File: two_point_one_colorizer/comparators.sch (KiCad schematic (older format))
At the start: 13 parts, among them U7 LM393

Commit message: revised all boards
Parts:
- RV1, RV2: value 10k -> 10k_pot
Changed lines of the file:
@@
 P 3875 2675
 F 0 "RV1" H 3805 2721 50  0000 R CNN
-F 1 "10k" H 3805 2630 50  0000 R CNN
+F 1 "10k_pot" H 3805 2630 50  0000 R CNN
 F 2 "lib_fp:Potentiometer_Vertical_Large" H 3875 2675 50  0001 C CNN
 F 3 "~" H 3875 2675 50  0001 C CNN
@@
 P 3825 5175
 F 0 "RV2" H 3755 5221 50  0000 R CNN
-F 1 "10k" H 3755 5130 50  0000 R CNN
+F 1 "10k_pot" H 3755 5130 50  0000 R CNN
 F 2 "lib_fp:Potentiometer_Vertical_Large" H 3825 5175 50  0001 C CNN
 F 3 "~" H 3825 5175 50  0001 C CNN

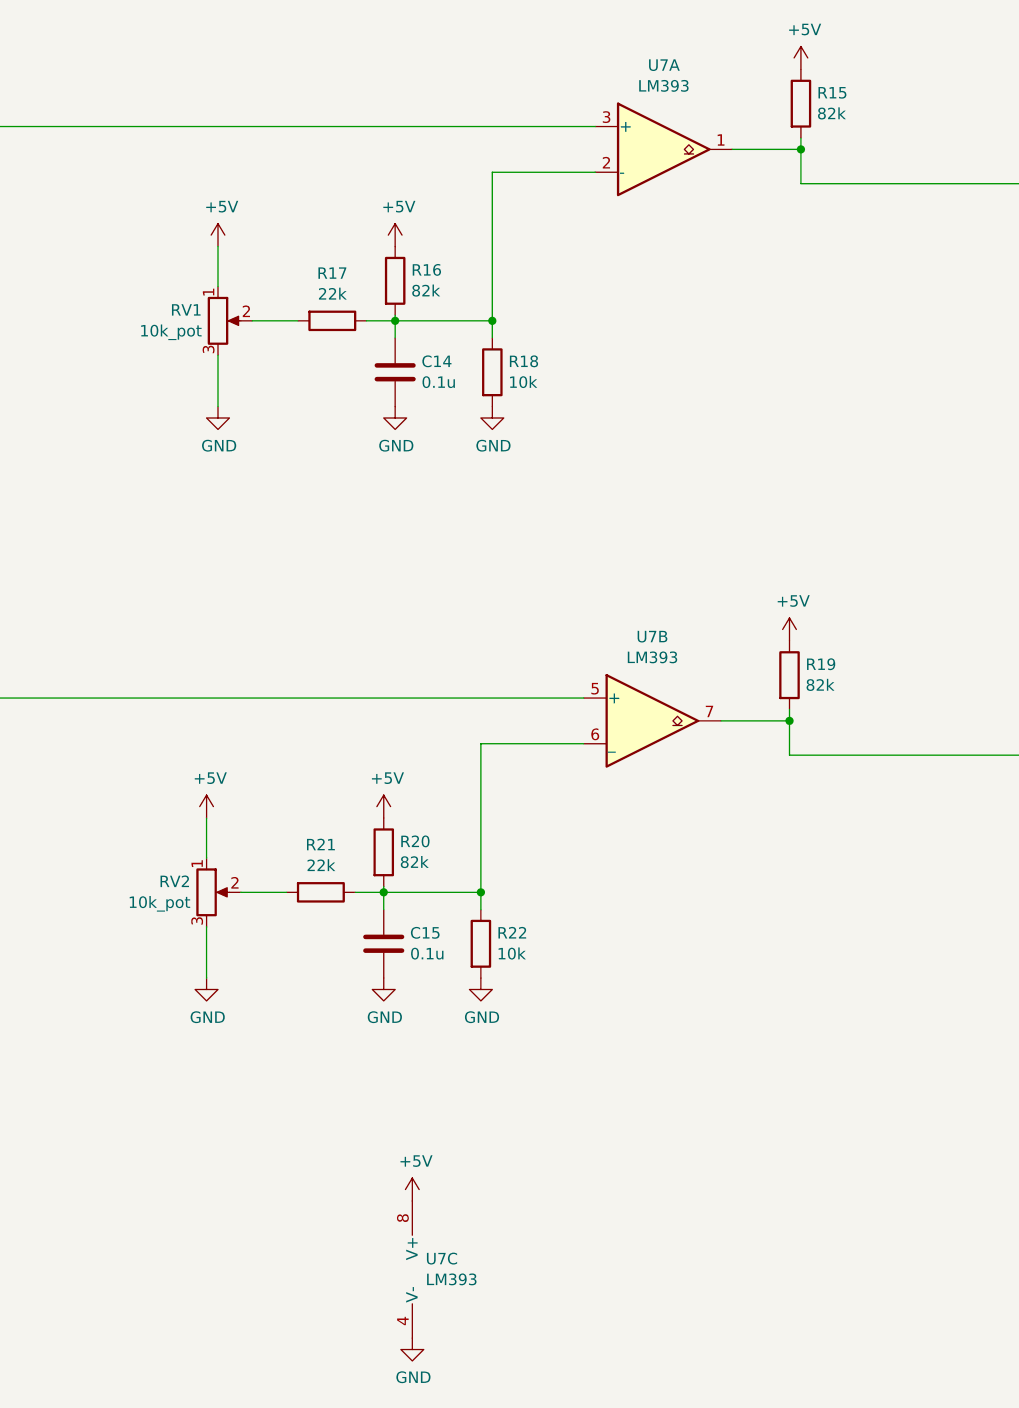
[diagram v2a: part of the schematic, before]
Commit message: lay out colorizer
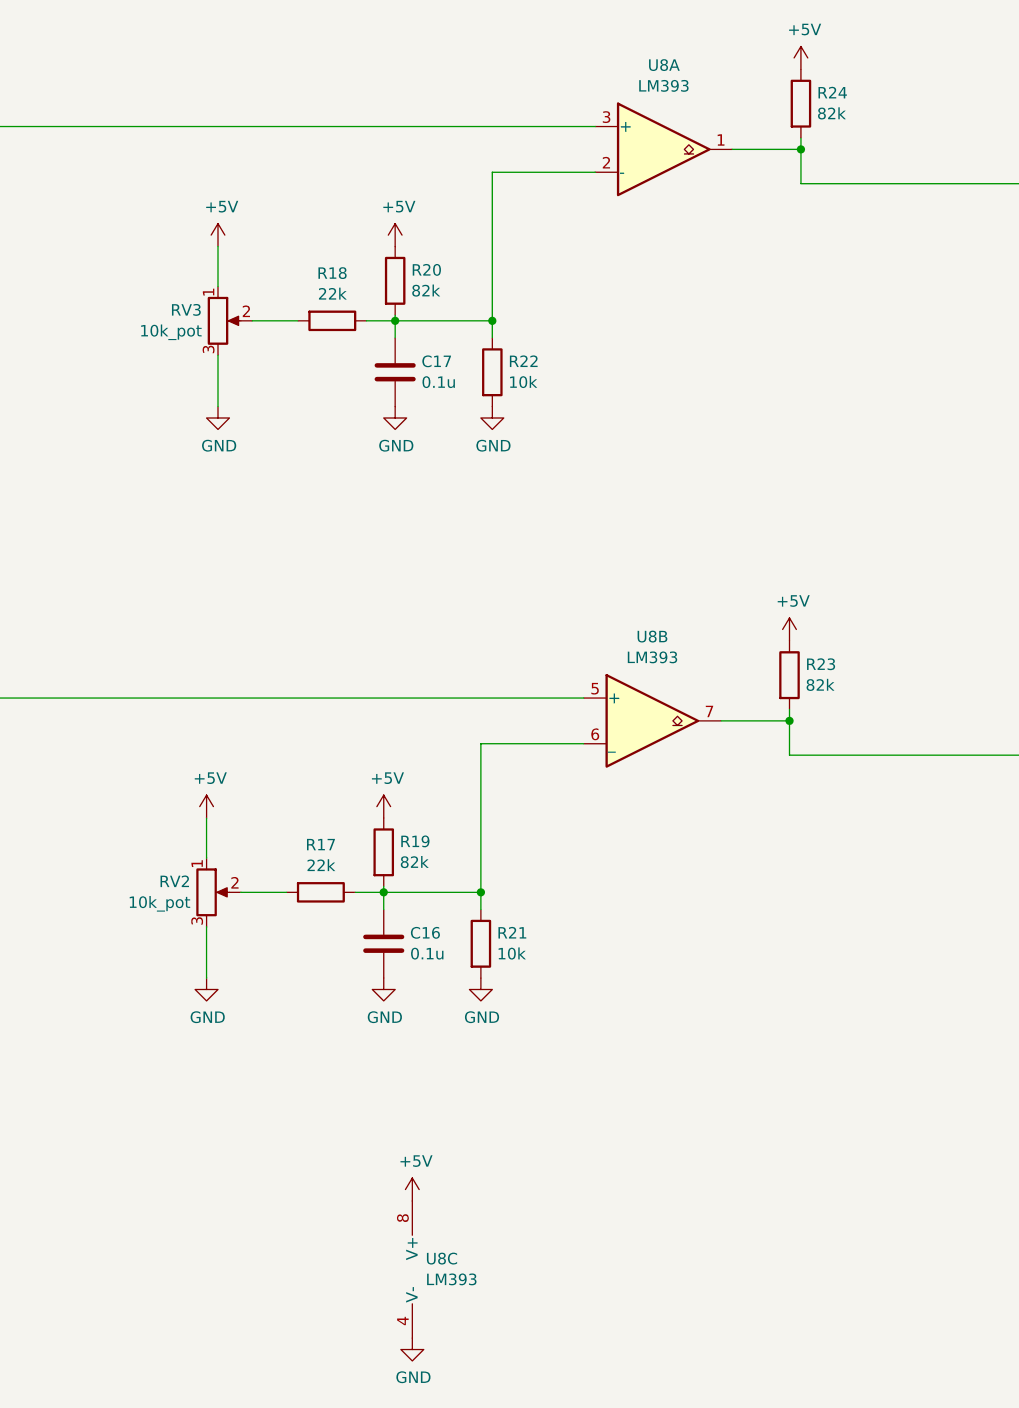
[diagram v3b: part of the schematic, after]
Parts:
- C16: renamed from C15; footprint Capacitor_THT:C_Disc_D4.7mm_W2.5mm_P5.00mm -> lib_fp:C_Disc_D4.7mm_W2.5mm_P5.00mm
- C17: renamed from C14; footprint Capacitor_THT:C_Disc_D4.7mm_W2.5mm_P5.00mm -> lib_fp:C_Disc_D4.7mm_W2.5mm_P5.00mm
- R17: renamed from R21; footprint Resistor_THT:R_Axial_DIN0207_L6.3mm_D2.5mm_P7.62mm_Horizontal -> lib_fp:R_Axial_DIN0207_L6.3mm_D2.5mm_P7.62mm_Horizontal
- R18: renamed from R17; footprint Resistor_THT:R_Axial_DIN0207_L6.3mm_D2.5mm_P7.62mm_Horizontal -> lib_fp:R_Axial_DIN0207_L6.3mm_D2.5mm_P7.62mm_Horizontal
- R19: renamed from R20; footprint Resistor_THT:R_Axial_DIN0207_L6.3mm_D2.5mm_P7.62mm_Horizontal -> lib_fp:R_Axial_DIN0207_L6.3mm_D2.5mm_P7.62mm_Horizontal
- R20: renamed from R16; footprint Resistor_THT:R_Axial_DIN0207_L6.3mm_D2.5mm_P7.62mm_Horizontal -> lib_fp:R_Axial_DIN0207_L6.3mm_D2.5mm_P7.62mm_Horizontal
- R21: renamed from R22; footprint Resistor_THT:R_Axial_DIN0207_L6.3mm_D2.5mm_P7.62mm_Horizontal -> lib_fp:R_Axial_DIN0207_L6.3mm_D2.5mm_P7.62mm_Horizontal
- R22: renamed from R18; footprint Resistor_THT:R_Axial_DIN0207_L6.3mm_D2.5mm_P7.62mm_Horizontal -> lib_fp:R_Axial_DIN0207_L6.3mm_D2.5mm_P7.62mm_Horizontal
- R23: renamed from R19; footprint Resistor_THT:R_Axial_DIN0207_L6.3mm_D2.5mm_P7.62mm_Horizontal -> lib_fp:R_Axial_DIN0207_L6.3mm_D2.5mm_P7.62mm_Horizontal
- R24: renamed from R15; footprint Resistor_THT:R_Axial_DIN0207_L6.3mm_D2.5mm_P7.62mm_Horizontal -> lib_fp:R_Axial_DIN0207_L6.3mm_D2.5mm_P7.62mm_Horizontal
- renumbered RV1 to RV3, U7 to U8
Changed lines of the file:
@@
 video
 $Comp
-L Device:R_POT RV1
+L Device:R_POT RV3
 U 1 1 5F2C6E9D
 P 3875 2675
-F 0 "RV1" H 3805 2721 50  0000 R CNN
+F 0 "RV3" H 3805 2721 50  0000 R CNN
 F 1 "10k_pot" H 3805 2630 50  0000 R CNN
 F 2 "lib_fp:Potentiometer_Vertical_Large" H 3875 2675 50  0001 C CNN
@@
 $EndComp
 $Comp
-L power:+5V #PWR043
+L power:+5V #PWR052
 U 1 1 5F2C7572
 P 3875 2350
-F 0 "#PWR043" H 3875 2200 50  0001 C CNN
+F 0 "#PWR052" H 3875 2200 50  0001 C CNN
 F 1 "+5V" H 3890 2523 50  0000 C CNN
 F 2 "" H 3875 2350 50  0001 C CNN
@@
 $EndComp
 $Comp
-L power:GND #PWR045
+L power:GND #PWR053
 U 1 1 5F2C80B8
 P 3875 3050
-F 0 "#PWR045" H 3875 2800 50  0001 C CNN
+F 0 "#PWR053" H 3875 2800 50  0001 C CNN
 F 1 "GND" H 3880 2877 50  0000 C CNN
 F 2 "" H 3875 3050 50  0001 C CNN
@@
 $EndComp
 $Comp
-L Device:R R17
+L Device:R R18
 U 1 1 5F2C8417
 P 4375 2675
-F 0 "R17" V 4168 2675 50  0000 C CNN
+F 0 "R18" V 4168 2675 50  0000 C CNN
 F 1 "22k" V 4259 2675 50  0000 C CNN
-F 2 "Resistor_THT:R_Axial_DIN0207_L6.3mm_D2.5mm_P7.62mm_Horizontal" V 4305 2675 50  0001 C CNN
+F 2 "lib_fp:R_Axial_DIN0207_L6.3mm_D2.5mm_P7.62mm_Horizontal" V 4305 2675 50  0001 C CNN
 F 3 "~" H 4375 2675 50  0001 C CNN
 	1    4375 2675
@@
 	4025 2675 4225 2675
 $Comp
-L Device:R R16
+L Device:R R20
 U 1 1 5F2C8A04
 P 4650 2500
-F 0 "R16" H 4720 2546 50  0000 L CNN
+F 0 "R20" H 4720 2546 50  0000 L CNN
 F 1 "82k" H 4720 2455 50  0000 L CNN
-F 2 "Resistor_THT:R_Axial_DIN0207_L6.3mm_D2.5mm_P7.62mm_Horizontal" V 4580 2500 50  0001 C CNN
+F 2 "lib_fp:R_Axial_DIN0207_L6.3mm_D2.5mm_P7.62mm_Horizontal" V 4580 2500 50  0001 C CNN
 F 3 "~" H 4650 2500 50  0001 C CNN
 	1    4650 2500
@@
 $EndComp
 $Comp
-L power:+5V #PWR044
+L power:+5V #PWR056
 U 1 1 5F2C8D77
 P 4650 2350
-F 0 "#PWR044" H 4650 2200 50  0001 C CNN
+F 0 "#PWR056" H 4650 2200 50  0001 C CNN
 F 1 "+5V" H 4665 2523 50  0000 C CNN
 F 2 "" H 4650 2350 50  0001 C CNN
@@
 	3875 2350 3875 2525
 $Comp
-L Device:C C14
+L Device:C C17
 U 1 1 5F2C9917
 P 4650 2900
-F 0 "C14" H 4765 2946 50  0000 L CNN
+F 0 "C17" H 4765 2946 50  0000 L CNN
 F 1 "0.1u" H 4765 2855 50  0000 L CNN
-F 2 "Capacitor_THT:C_Disc_D4.7mm_W2.5mm_P5.00mm" H 4688 2750 50  0001 C CNN
+F 2 "lib_fp:C_Disc_D4.7mm_W2.5mm_P5.00mm" H 4688 2750 50  0001 C CNN
 F 3 "~" H 4650 2900 50  0001 C CNN
 	1    4650 2900
@@
 $EndComp
 $Comp
-L power:GND #PWR046
+L power:GND #PWR057
 U 1 1 5F2C9CEF
 P 4650 3050
-F 0 "#PWR046" H 4650 2800 50  0001 C CNN
+F 0 "#PWR057" H 4650 2800 50  0001 C CNN
 F 1 "GND" H 4655 2877 50  0000 C CNN
 F 2 "" H 4650 3050 50  0001 C CNN
@@
 	3875 2825 3875 3050
 $Comp
-L Device:R R18
+L Device:R R22
 U 1 1 5F2CA577
 P 5075 2900
-F 0 "R18" H 5145 2946 50  0000 L CNN
+F 0 "R22" H 5145 2946 50  0000 L CNN
 F 1 "10k" H 5145 2855 50  0000 L CNN
-F 2 "Resistor_THT:R_Axial_DIN0207_L6.3mm_D2.5mm_P7.62mm_Horizontal" V 5005 2900 50  0001 C CNN
+F 2 "lib_fp:R_Axial_DIN0207_L6.3mm_D2.5mm_P7.62mm_Horizontal" V 5005 2900 50  0001 C CNN
 F 3 "~" H 5075 2900 50  0001 C CNN
 	1    5075 2900
@@
 $EndComp
 $Comp
-L power:GND #PWR047
+L power:GND #PWR061
 U 1 1 5F2CAB02
 P 5075 3050
-F 0 "#PWR047" H 5075 2800 50  0001 C CNN
+F 0 "#PWR061" H 5075 2800 50  0001 C CNN
 F 1 "GND" H 5080 2877 50  0000 C CNN
 F 2 "" H 5075 3050 50  0001 C CNN
@@
 Connection ~ 5075 2675
 $Comp
-L Device:R R15
+L Device:R R24
 U 1 1 5F2CE620
 P 6425 1725
-F 0 "R15" H 6495 1771 50  0000 L CNN
+F 0 "R24" H 6495 1771 50  0000 L CNN
 F 1 "82k" H 6495 1680 50  0000 L CNN
-F 2 "Resistor_THT:R_Axial_DIN0207_L6.3mm_D2.5mm_P7.62mm_Horizontal" V 6355 1725 50  0001 C CNN
+F 2 "lib_fp:R_Axial_DIN0207_L6.3mm_D2.5mm_P7.62mm_Horizontal" V 6355 1725 50  0001 C CNN
 F 3 "~" H 6425 1725 50  0001 C CNN
 	1    6425 1725
@@
 $EndComp
 $Comp
-L power:+5V #PWR042
+L power:+5V #PWR063
 U 1 1 5F2CEE7B
 P 6425 1575
-F 0 "#PWR042" H 6425 1425 50  0001 C CNN
+F 0 "#PWR063" H 6425 1425 50  0001 C CNN
 F 1 "+5V" H 6440 1748 50  0000 C CNN
 F 2 "" H 6425 1575 50  0001 C CNN
@@
 $EndComp
 $Comp
-L power:+5V #PWR049
+L power:+5V #PWR050
 U 1 1 5F2D3154
 P 3825 4850
-F 0 "#PWR049" H 3825 4700 50  0001 C CNN
+F 0 "#PWR050" H 3825 4700 50  0001 C CNN
 F 1 "+5V" H 3840 5023 50  0000 C CNN
 F 2 "" H 3825 4850 50  0001 C CNN
@@
 $EndComp
 $Comp
-L Device:R R21
+L Device:R R17
 U 1 1 5F2D3168
 P 4325 5175
-F 0 "R21" V 4118 5175 50  0000 C CNN
+F 0 "R17" V 4118 5175 50  0000 C CNN
 F 1 "22k" V 4209 5175 50  0000 C CNN
-F 2 "Resistor_THT:R_Axial_DIN0207_L6.3mm_D2.5mm_P7.62mm_Horizontal" V 4255 5175 50  0001 C CNN
+F 2 "lib_fp:R_Axial_DIN0207_L6.3mm_D2.5mm_P7.62mm_Horizontal" V 4255 5175 50  0001 C CNN
 F 3 "~" H 4325 5175 50  0001 C CNN
 	1    4325 5175
@@
 	3975 5175 4175 5175
 $Comp
-L Device:R R20
+L Device:R R19
 U 1 1 5F2D3173
 P 4600 5000
-F 0 "R20" H 4670 5046 50  0000 L CNN
+F 0 "R19" H 4670 5046 50  0000 L CNN
 F 1 "82k" H 4670 4955 50  0000 L CNN
-F 2 "Resistor_THT:R_Axial_DIN0207_L6.3mm_D2.5mm_P7.62mm_Horizontal" V 4530 5000 50  0001 C CNN
+F 2 "lib_fp:R_Axial_DIN0207_L6.3mm_D2.5mm_P7.62mm_Horizontal" V 4530 5000 50  0001 C CNN
 F 3 "~" H 4600 5000 50  0001 C CNN
 	1    4600 5000
@@
 $EndComp
 $Comp
-L power:+5V #PWR050
+L power:+5V #PWR054
 U 1 1 5F2D317D
 P 4600 4850
-F 0 "#PWR050" H 4600 4700 50  0001 C CNN
+F 0 "#PWR054" H 4600 4700 50  0001 C CNN
 F 1 "+5V" H 4615 5023 50  0000 C CNN
 F 2 "" H 4600 4850 50  0001 C CNN
@@
 	3825 4850 3825 5025
 $Comp
-L Device:C C15
+L Device:C C16
 U 1 1 5F2D3188
 P 4600 5400
-F 0 "C15" H 4715 5446 50  0000 L CNN
+F 0 "C16" H 4715 5446 50  0000 L CNN
 F 1 "0.1u" H 4715 5355 50  0000 L CNN
-F 2 "Capacitor_THT:C_Disc_D4.7mm_W2.5mm_P5.00mm" H 4638 5250 50  0001 C CNN
+F 2 "lib_fp:C_Disc_D4.7mm_W2.5mm_P5.00mm" H 4638 5250 50  0001 C CNN
 F 3 "~" H 4600 5400 50  0001 C CNN
 	1    4600 5400
@@
 $EndComp
 $Comp
-L power:GND #PWR052
+L power:GND #PWR055
 U 1 1 5F2D3192
 P 4600 5550
-F 0 "#PWR052" H 4600 5300 50  0001 C CNN
+F 0 "#PWR055" H 4600 5300 50  0001 C CNN
 F 1 "GND" H 4605 5377 50  0000 C CNN
 F 2 "" H 4600 5550 50  0001 C CNN
@@
 	3825 5325 3825 5550
 $Comp
-L Device:R R22
+L Device:R R21
 U 1 1 5F2D319D
 P 5025 5400
-F 0 "R22" H 5095 5446 50  0000 L CNN
+F 0 "R21" H 5095 5446 50  0000 L CNN
 F 1 "10k" H 5095 5355 50  0000 L CNN
-F 2 "Resistor_THT:R_Axial_DIN0207_L6.3mm_D2.5mm_P7.62mm_Horizontal" V 4955 5400 50  0001 C CNN
+F 2 "lib_fp:R_Axial_DIN0207_L6.3mm_D2.5mm_P7.62mm_Horizontal" V 4955 5400 50  0001 C CNN
 F 3 "~" H 5025 5400 50  0001 C CNN
 	1    5025 5400
@@
 $EndComp
 $Comp
-L power:GND #PWR053
+L power:GND #PWR060
 U 1 1 5F2D31A7
 P 5025 5550
-F 0 "#PWR053" H 5025 5300 50  0001 C CNN
+F 0 "#PWR060" H 5025 5300 50  0001 C CNN
 F 1 "GND" H 5030 5377 50  0000 C CNN
 F 2 "" H 5025 5550 50  0001 C CNN
@@
 Connection ~ 5025 5175
 $Comp
-L Device:R R19
+L Device:R R23
 U 1 1 5F2D31DC
 P 6375 4225
-F 0 "R19" H 6445 4271 50  0000 L CNN
+F 0 "R23" H 6445 4271 50  0000 L CNN
 F 1 "82k" H 6445 4180 50  0000 L CNN
-F 2 "Resistor_THT:R_Axial_DIN0207_L6.3mm_D2.5mm_P7.62mm_Horizontal" V 6305 4225 50  0001 C CNN
+F 2 "lib_fp:R_Axial_DIN0207_L6.3mm_D2.5mm_P7.62mm_Horizontal" V 6305 4225 50  0001 C CNN
 F 3 "~" H 6375 4225 50  0001 C CNN
 	1    6375 4225
@@
 $EndComp
 $Comp
-L power:+5V #PWR048
+L power:+5V #PWR062
 U 1 1 5F2D31E6
 P 6375 4075
-F 0 "#PWR048" H 6375 3925 50  0001 C CNN
+F 0 "#PWR062" H 6375 3925 50  0001 C CNN
 F 1 "+5V" H 6390 4248 50  0000 C CNN
 F 2 "" H 6375 4075 50  0001 C CNN
@@
 Connection ~ 2050 1825
 $Comp
-L Comparator:LM393 U7
+L Comparator:LM393 U8
 U 1 1 5F2DA04B
 P 5825 1925
-F 0 "U7" H 5825 2292 50  0000 C CNN
+F 0 "U8" H 5825 2292 50  0000 C CNN
 F 1 "LM393" H 5825 2201 50  0000 C CNN
 F 2 "Package_DIP:DIP-8_W7.62mm_LongPads" H 5825 1925 50  0001 C CNN
@@
 $EndComp
 $Comp
-L Comparator:LM393 U7
+L Comparator:LM393 U8
 U 2 1 5F2DC03F
 P 5775 4425
-F 0 "U7" H 5775 4792 50  0000 C CNN
+F 0 "U8" H 5775 4792 50  0000 C CNN
 F 1 "LM393" H 5775 4701 50  0000 C CNN
 F 2 "Package_DIP:DIP-8_W7.62mm_LongPads" H 5775 4425 50  0001 C CNN
@@
 $EndComp
 $Comp
-L Comparator:LM393 U7
+L Comparator:LM393 U8
 U 3 1 5F2DDE9E
 P 4825 6825
-F 0 "U7" H 4783 6871 50  0000 L CNN
+F 0 "U8" H 4783 6871 50  0000 L CNN
 F 1 "LM393" H 4783 6780 50  0000 L CNN
 F 2 "Package_DIP:DIP-8_W7.62mm_LongPads" H 4825 6825 50  0001 C CNN
@@
 $EndComp
 $Comp
-L power:+5V #PWR039
+L power:+5V #PWR058
 U 1 1 5F2DEBAE
 P 4725 6525
-F 0 "#PWR039" H 4725 6375 50  0001 C CNN
+F 0 "#PWR058" H 4725 6375 50  0001 C CNN
 F 1 "+5V" H 4740 6698 50  0000 C CNN
 F 2 "" H 4725 6525 50  0001 C CNN
@@
 $EndComp
 $Comp
-L power:GND #PWR040
+L power:GND #PWR059
 U 1 1 5F2DF1FD
 P 4725 7125
-F 0 "#PWR040" H 4725 6875 50  0001 C CNN
+F 0 "#PWR059" H 4725 6875 50  0001 C CNN
 F 1 "GND" H 4730 6952 50  0000 C CNN
 F 2 "" H 4725 7125 50  0001 C CNN

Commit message: updates
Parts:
- removed R21, R22: 10k, lib_fp:R_Axial_DIN0207_L6.3mm_D2.5mm_P7.62mm_Horizontal, symbol Device:R
- R17, R18: value 22k -> 18k
- R19, R20: value 82k -> 22k
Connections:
- net +5V: no longer RV2.1, RV3.1
- net GND: now also R17.1, R18.1; no longer RV2.3, RV3.3
- net at RV3.2: now also C17.1, U8.2 (-); no longer R18.2
- net at RV2.2: now also C16.1, U8.6 (_); no longer R17.2
- new net: R20.2, RV3.1
- new net: R18.2, RV3.3
- new net: R19.2, RV2.1
- new net: R17.2, RV2.3
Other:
- moved on the sheet: C16, C17, R17, R18, R19, R20, R23, R24, RV2, RV3, U8A, U8B
